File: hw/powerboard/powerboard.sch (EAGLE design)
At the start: 39 parts, among them J1 ISP, J2 I2C, Q1 IRF4905

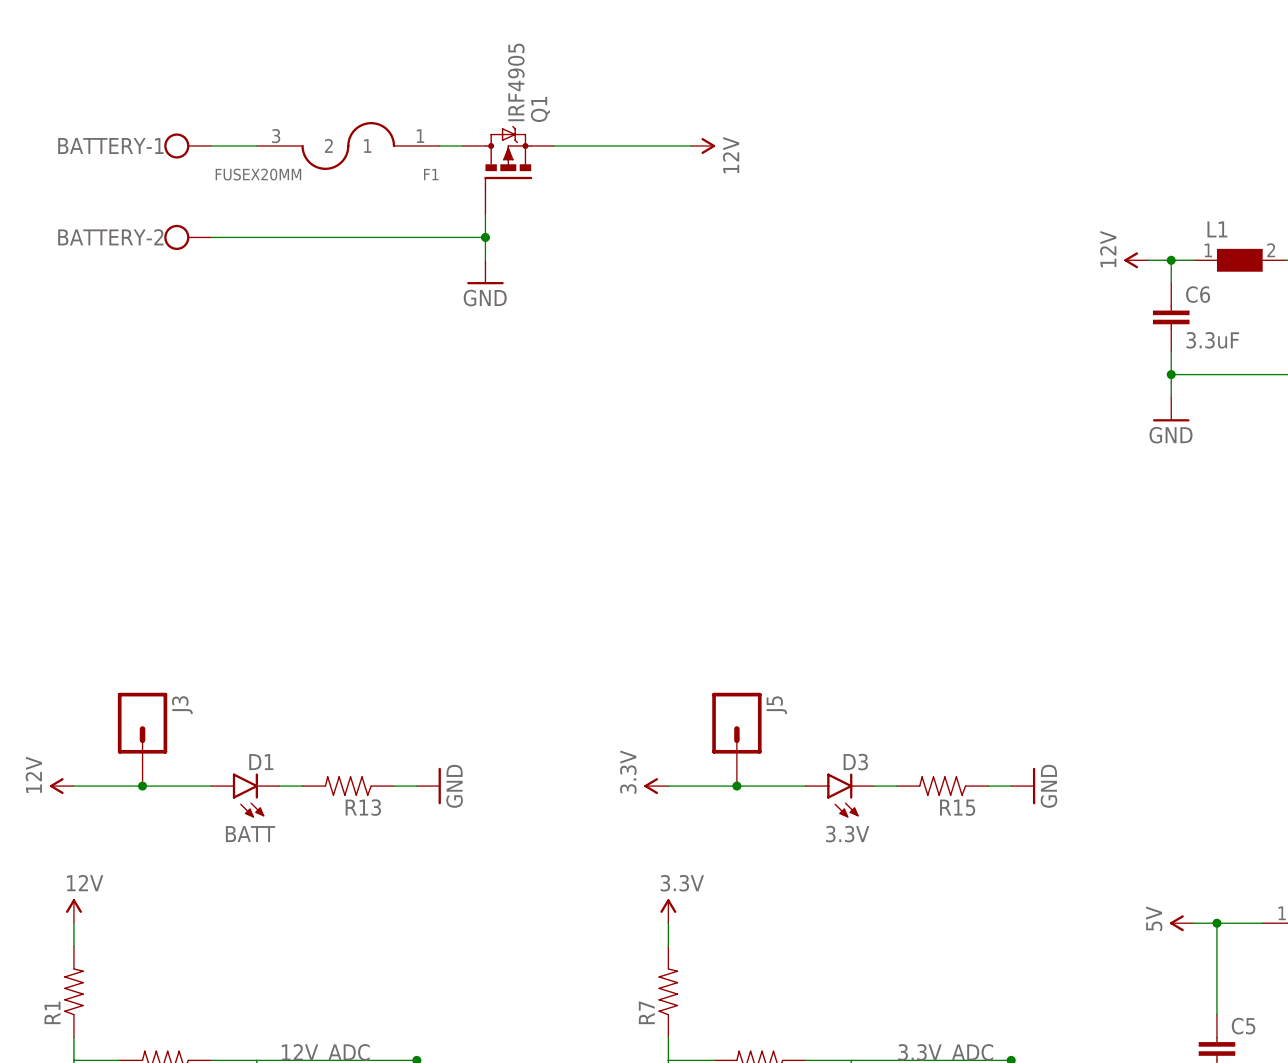
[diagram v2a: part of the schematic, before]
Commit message: Added N-channel MOSFET and TVS-diode to powerboard
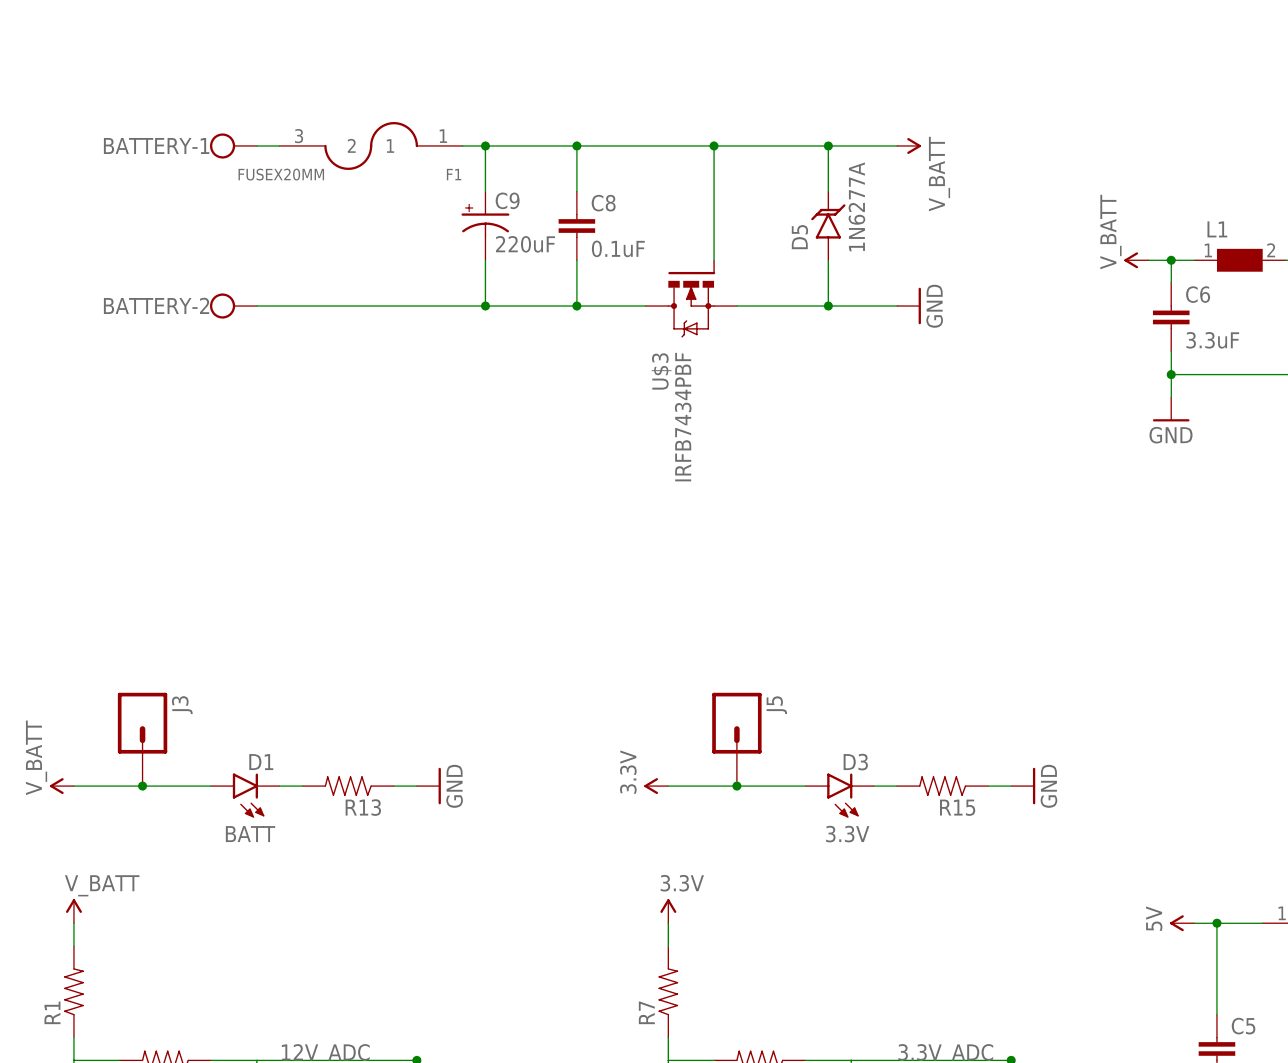
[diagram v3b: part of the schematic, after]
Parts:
- removed Q1: IRF4905, transistor-power:IRF4905
- added C8: 0.1uF, SparkFun-Capacitors:0.1UF-25V-5%(0603)
- added C9: 220uF, rcl:CPOL-USG
- added D5: 1N6277A, powerboard:1N6277A
- added U$3: IRFB7434PBF, powerboard:IRFB7434PBF
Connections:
- removed net 12V: C6.1, D1.A, J3.1, L1.1, Q1.S, R1.2
- removed net N$9: F1.1, Q1.D
- new net N$12: BATTERY-2.KL, C8.2, C9.-, U$3.D
- new net V_BATT: C6.1, C8.1, C9.+, D1.A, D5.C, F1.1, J3.1, L1.1, R1.2, U$3.G
- net GND: now also D5.A, U$3.S; no longer BATTERY-2.KL, Q1.G
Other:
- moved on the sheet: BATTERY-1, BATTERY-2, F1
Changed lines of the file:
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@@
 <part name="GND14" library="SparkFun-Aesthetics" deviceset="GND" device=""/>
 <part name="U$2" library="powerboard" deviceset="AXA04AXX-L" device=""/>
-<part name="SUPPLY14" library="SparkFun-Aesthetics" deviceset="12V" device=""/>
-<part name="SUPPLY8" library="SparkFun-Aesthetics" deviceset="12V" device=""/>
-<part name="SUPPLY13" library="SparkFun-Aesthetics" deviceset="12V" device=""/>
-<part name="SUPPLY2" library="SparkFun-Aesthetics" deviceset="12V" device=""/>
-<part name="Q1" library="transistor-power" deviceset="IRF4905" device=""/>
 <part name="GND6" library="SparkFun-Aesthetics" deviceset="GND" device=""/>
 <part name="BATTERY" library="con-wago-500" deviceset="W237-102" device=""/>
+<part name="C8" library="SparkFun-Capacitors" deviceset="0.1UF-25V-5%(0603)" device="" value="0.1uF"/>
+<part name="C9" library="rcl" deviceset="CPOL-US" device="G" value="220uF"/>
+<part name="D5" library="powerboard" deviceset="1N6277A" device="" value="1N6277A"/>
+<part name="SUPPLY6" library="SparkFun-Aesthetics" deviceset="V_BATT" device=""/>
+<part name="SUPPLY8" library="SparkFun-Aesthetics" deviceset="V_BATT" device=""/>
+<part name="SUPPLY13" library="SparkFun-Aesthetics" deviceset="V_BATT" device=""/>
+<part name="SUPPLY2" library="SparkFun-Aesthetics" deviceset="V_BATT" device=""/>
+<part name="U$3" library="powerboard" deviceset="IRFB7434PBF" device=""/>
 </parts>
 <sheets>
@@
 <instance part="C4" gate="G$1" x="114.3" y="60.96"/>
 <instance part="C5" gate="G$1" x="154.94" y="144.78"/>
-<instance part="F1" gate="G$1" x="58.42" y="246.38" rot="R180"/>
+<instance part="F1" gate="G$1" x="60.96" y="246.38" rot="R180"/>
 <instance part="SUPPLY4" gate="G$1" x="27.94" y="86.36"/>
 <instance part="SUPPLY3" gate="G$1" x="93.98" y="86.36"/>
@@
 <instance part="GND14" gate="1" x="149.86" y="215.9"/>
 <instance part="U$2" gate="G$1" x="172.72" y="238.76"/>
-<instance part="SUPPLY14" gate="G$1" x="96.52" y="246.38" rot="R270"/>
+<instance part="GND6" gate="1" x="121.92" y="228.6" rot="R90"/>
+<instance part="BATTERY" gate="-1" x="43.18" y="246.38"/>
+<instance part="BATTERY" gate="-2" x="43.18" y="228.6"/>
+<instance part="C8" gate="G$1" x="83.82" y="236.22"/>
+<instance part="C9" gate="G$1" x="73.66" y="238.76"/>
+<instance part="D5" gate="G$1" x="111.76" y="236.22" rot="R90"/>
+<instance part="SUPPLY6" gate="G$1" x="119.38" y="246.38" rot="R270"/>
 <instance part="SUPPLY8" gate="G$1" x="147.32" y="233.68" rot="R90"/>
 <instance part="SUPPLY13" gate="G$1" x="27.94" y="175.26" rot="R90"/>
 <instance part="SUPPLY2" gate="G$1" x="27.94" y="160.02"/>
-<instance part="Q1" gate="G$1" x="76.2" y="243.84" rot="MR90"/>
-<instance part="GND6" gate="1" x="73.66" y="231.14"/>
-<instance part="BATTERY" gate="-1" x="38.1" y="246.38"/>
-<instance part="BATTERY" gate="-2" x="38.1" y="236.22"/>
+<instance part="U$3" gate="G$1" x="96.52" y="231.14" rot="MR270"/>
 </instances>
 <busses>
@@
 </segment>
 <segment>
-<pinref part="Q1" gate="G$1" pin="G"/>
 <pinref part="GND6" gate="1" pin="GND"/>
-<wire x1="73.66" y1="238.76" x2="73.66" y2="236.22" width="0.1524" layer="91"/>
-<pinref part="BATTERY" gate="-2" pin="KL"/>
-<wire x1="73.66" y1="236.22" x2="73.66" y2="233.68" width="0.1524" layer="91"/>
-<wire x1="43.18" y1="236.22" x2="73.66" y2="236.22" width="0.1524" layer="91"/>
-<junction x="73.66" y="236.22"/>
+<pinref part="D5" gate="G$1" pin="A"/>
+<wire x1="111.76" y1="228.6" x2="119.38" y2="228.6" width="0.1524" layer="91"/>
+<wire x1="111.76" y1="233.68" x2="111.76" y2="228.6" width="0.1524" layer="91"/>
+<wire x1="101.6" y1="228.6" x2="111.76" y2="228.6" width="0.1524" layer="91"/>
+<junction x="111.76" y="228.6"/>
+<pinref part="U$3" gate="G$1" pin="S"/>
 </segment>
 </net>
@@
 </segment>
 </net>
-<net name="12V" class="0">
-<segment>
-<pinref part="L1" gate="G$1" pin="1"/>
-<pinref part="C6" gate="G$1" pin="1"/>
-<wire x1="152.4" y1="233.68" x2="149.86" y2="233.68" width="0.1524" layer="91"/>
-<wire x1="149.86" y1="233.68" x2="149.86" y2="231.14" width="0.1524" layer="91"/>
-<wire x1="149.86" y1="233.68" x2="147.32" y2="233.68" width="0.1524" layer="91"/>
-<junction x="149.86" y="233.68"/>
-<pinref part="SUPPLY8" gate="G$1" pin="12V"/>
-</segment>
-<segment>
-<pinref part="D1" gate="G$1" pin="A"/>
-<wire x1="27.94" y1="175.26" x2="35.56" y2="175.26" width="0.1524" layer="91"/>
-<pinref part="J3" gate="G$1" pin="1"/>
-<wire x1="35.56" y1="175.26" x2="43.18" y2="175.26" width="0.1524" layer="91"/>
-<junction x="35.56" y="175.26"/>
-<pinref part="SUPPLY13" gate="G$1" pin="12V"/>
-</segment>
-<segment>
-<pinref part="R1" gate="G$1" pin="2"/>
-<wire x1="27.94" y1="157.48" x2="27.94" y2="160.02" width="0.1524" layer="91"/>
-<pinref part="SUPPLY2" gate="G$1" pin="12V"/>
-</segment>
-<segment>
-<pinref part="Q1" gate="G$1" pin="S"/>
-<pinref part="SUPPLY14" gate="G$1" pin="12V"/>
-<wire x1="81.28" y1="246.38" x2="96.52" y2="246.38" width="0.1524" layer="91"/>
-</segment>
-</net>
 <net name="12V_ADC" class="0">
 <segment>
@@
 </segment>
 </net>
-<net name="N$9" class="0">
-<segment>
-<pinref part="F1" gate="G$1" pin="1"/>
-<pinref part="Q1" gate="G$1" pin="D"/>
-<wire x1="68.58" y1="246.38" x2="71.12" y2="246.38" width="0.1524" layer="91"/>
-</segment>
-</net>
 <net name="N$11" class="0">
 <segment>
 <pinref part="BATTERY" gate="-1" pin="KL"/>
 <pinref part="F1" gate="G$1" pin="2"/>
-<wire x1="43.18" y1="246.38" x2="48.26" y2="246.38" width="0.1524" layer="91"/>
-</segment>
-</net>
+<wire x1="48.26" y1="246.38" x2="50.8" y2="246.38" width="0.1524" layer="91"/>
+</segment>
+</net>
+<net name="N$12" class="0">
+<segment>
+<pinref part="BATTERY" gate="-2" pin="KL"/>
+<wire x1="48.26" y1="228.6" x2="73.66" y2="228.6" width="0.1524" layer="91"/>
+<pinref part="C9" gate="G$1" pin="-"/>
+<wire x1="73.66" y1="228.6" x2="83.82" y2="228.6" width="0.1524" layer="91"/>
+<wire x1="73.66" y1="233.68" x2="73.66" y2="228.6" width="0.1524" layer="91"/>
+<junction x="73.66" y="228.6"/>
+<pinref part="C8" gate="G$1" pin="2"/>
+<wire x1="83.82" y1="233.68" x2="83.82" y2="228.6" width="0.1524" layer="91"/>
+<wire x1="83.82" y1="228.6" x2="91.44" y2="228.6" width="0.1524" layer="91"/>
+<junction x="83.82" y="228.6"/>
+<pinref part="U$3" gate="G$1" pin="D"/>
+</segment>
+</net>
+<net name="V_BATT" class="0">
+<segment>
+<pinref part="F1" gate="G$1" pin="1"/>
+<wire x1="71.12" y1="246.38" x2="73.66" y2="246.38" width="0.1524" layer="91"/>
+<pinref part="C9" gate="G$1" pin="+"/>
+<wire x1="73.66" y1="246.38" x2="83.82" y2="246.38" width="0.1524" layer="91"/>
+<wire x1="73.66" y1="241.3" x2="73.66" y2="246.38" width="0.1524" layer="91"/>
+<junction x="73.66" y="246.38"/>
+<pinref part="C8" gate="G$1" pin="1"/>
+<wire x1="83.82" y1="241.3" x2="83.82" y2="246.38" width="0.1524" layer="91"/>
+<junction x="83.82" y="246.38"/>
+<pinref part="SUPPLY6" gate="G$1" pin="V_BATT"/>
+<wire x1="83.82" y1="246.38" x2="99.06" y2="246.38" width="0.1524" layer="91"/>
+<pinref part="D5" gate="G$1" pin="C"/>
+<wire x1="99.06" y1="246.38" x2="111.76" y2="246.38" width="0.1524" layer="91"/>
+<wire x1="111.76" y1="246.38" x2="119.38" y2="246.38" width="0.1524" layer="91"/>
+<wire x1="111.76" y1="241.3" x2="111.76" y2="246.38" width="0.1524" layer="91"/>
+<junction x="111.76" y="246.38"/>
+<wire x1="99.06" y1="233.68" x2="99.06" y2="246.38" width="0.1524" layer="91"/>
+<junction x="99.06" y="246.38"/>
+<pinref part="U$3" gate="G$1" pin="G"/>
+</segment>
+<segment>
+<pinref part="L1" gate="G$1" pin="1"/>
+<pinref part="C6" gate="G$1" pin="1"/>
+<wire x1="152.4" y1="233.68" x2="149.86" y2="233.68" width="0.1524" layer="91"/>
+<wire x1="149.86" y1="233.68" x2="149.86" y2="231.14" width="0.1524" layer="91"/>
+<wire x1="149.86" y1="233.68" x2="147.32" y2="233.68" width="0.1524" layer="91"/>
+<junction x="149.86" y="233.68"/>
+<pinref part="SUPPLY8" gate="G$1" pin="V_BATT"/>
+</segment>
+<segment>
+<pinref part="D1" gate="G$1" pin="A"/>
+<wire x1="27.94" y1="175.26" x2="35.56" y2="175.26" width="0.1524" layer="91"/>
+<pinref part="J3" gate="G$1" pin="1"/>
+<wire x1="35.56" y1="175.26" x2="43.18" y2="175.26" width="0.1524" layer="91"/>
+<junction x="35.56" y="175.26"/>
+<pinref part="SUPPLY13" gate="G$1" pin="V_BATT"/>
+</segment>
+<segment>
+<pinref part="R1" gate="G$1" pin="2"/>
+<wire x1="27.94" y1="157.48" x2="27.94" y2="160.02" width="0.1524" layer="91"/>
+<pinref part="SUPPLY2" gate="G$1" pin="V_BATT"/>
+</segment>
+</net>
